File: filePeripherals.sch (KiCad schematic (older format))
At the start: 18 parts, among them J2 PP1_receptacle_TE_5-5530843-4, J3 PP1_receptacle_TE_5-5530843-4, J4 PP1_receptacle_TE_5-5530843-4, J5 PP1_receptacle_TE_5-5530843-4, U6 CD74AC238, U7 74AHC138

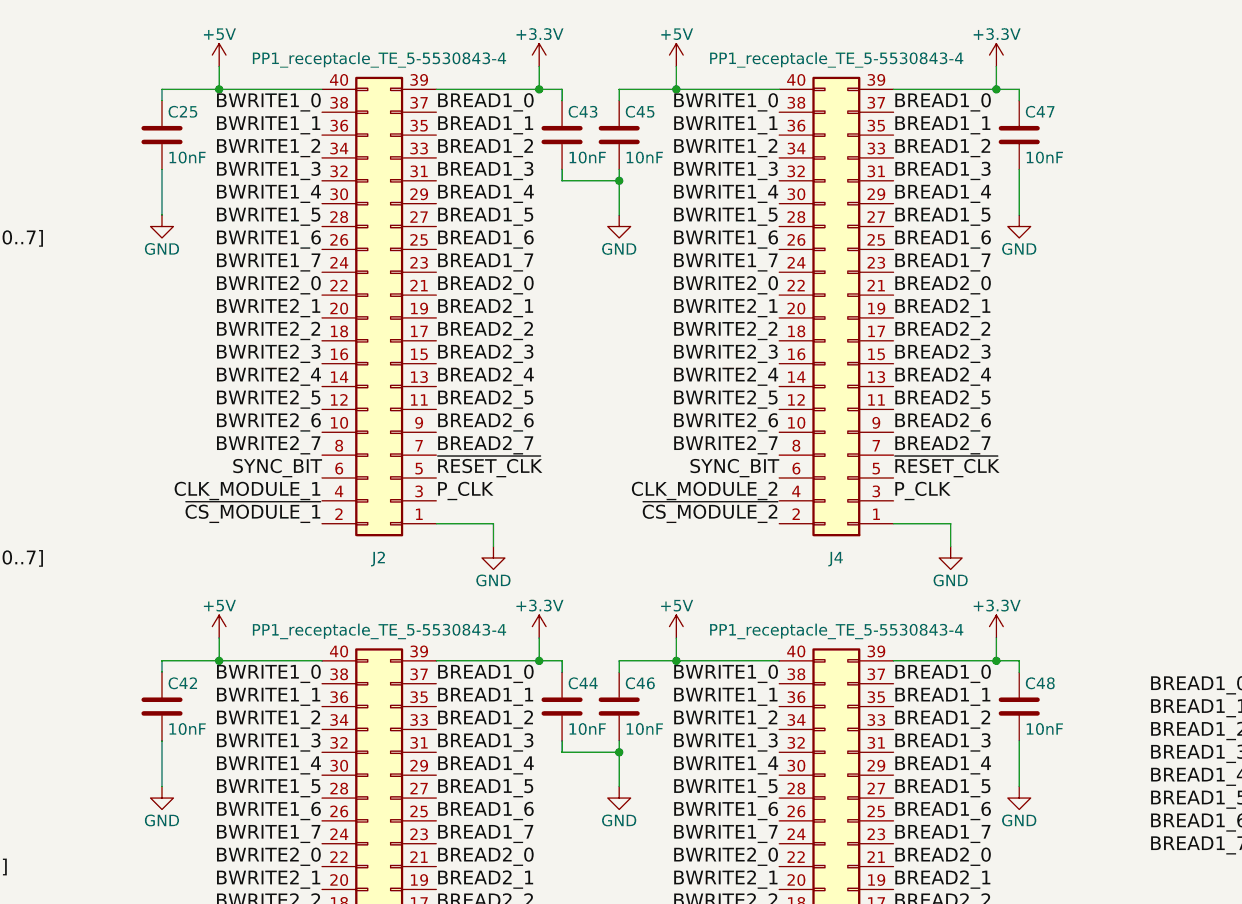
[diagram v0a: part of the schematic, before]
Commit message: V5.1 (#15)
* Remove compatibility for 5.0, 4.x and add 5.1+

* Fix switched pins on SN74LV393A #7

* Removed capacitor on 12V #11

* Add/Modify power decoupling capacitor #10

* Removing ADDSCR_CLK delay #9

* Schematics : set version 5.1, 2021 copyright and publish date

* Put non-electrolytic capacitor #10

* Set every capacitor size to 0805

* Add new footprint for J7 TE_3-641124-6 #6

* Schematic : set pinHeader on J12 #4

* Netlist, apply change to board, clean track, #6 #4 #12 #10

* Set version to 5.1, 2021 copyright and date, replace the missing QRcode

* Back the MM1 connectors #8

* Replace capacitor for U22 U23 U24 #13

* Better decoupling

* Increase version, year to 2021, clear status

* Precise the molex connector for power supply

* First step, import ses

* Clean bottom layer

* #14 Set the BWRITE2 bus instead of BWRITE1 on U12

* netlist, redo autorouting and cleaning

* use shields.io for colored badge

* Update gerbert files

* Changelog, updated BOM

* Small revision on blockDiagram

* Update README.md

* exporting pcb in pdf

* 3D images, diagram.png

* Update schematics pdf

* redo wavedrom_24bitsCounter
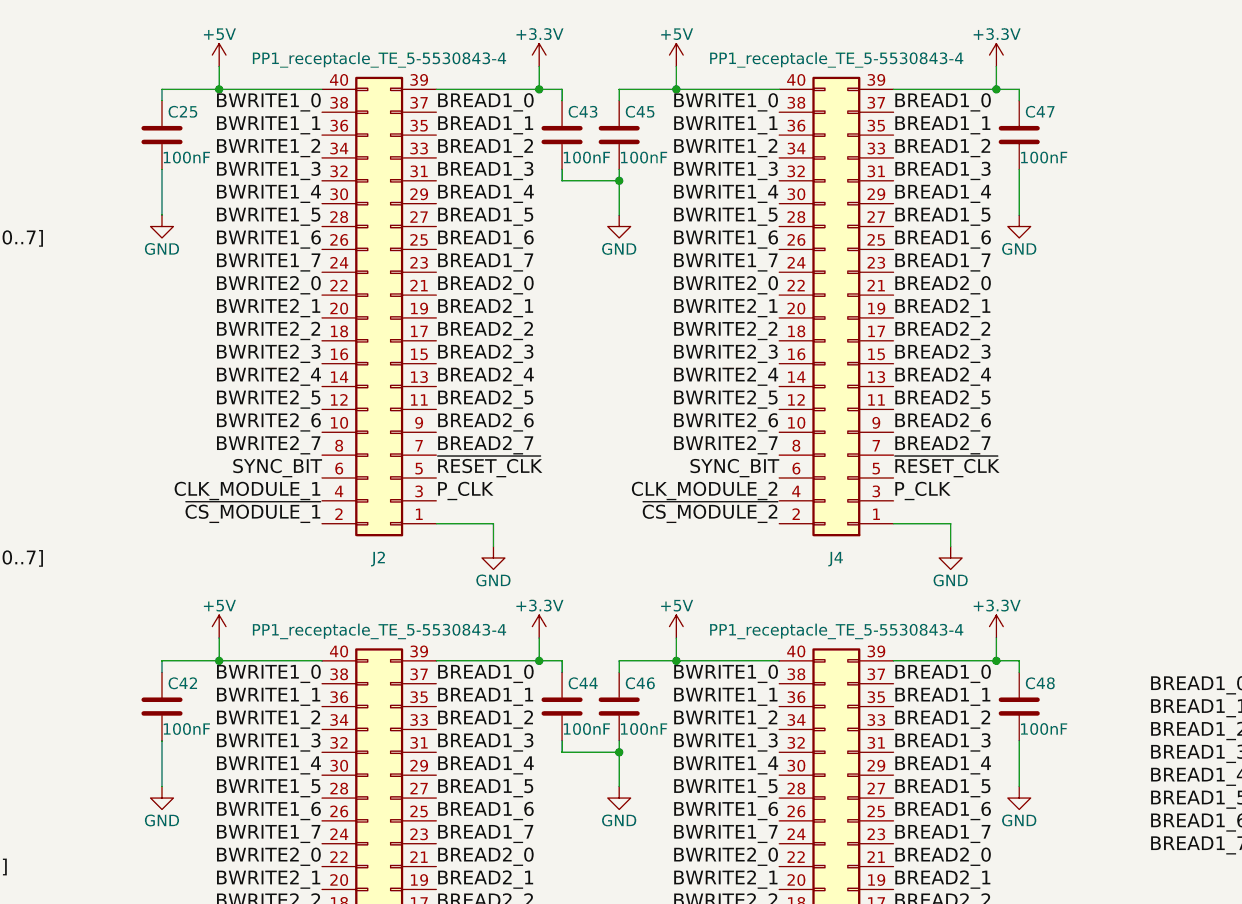
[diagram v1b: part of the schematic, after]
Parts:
- C25, C42, C43, C44, C45, C46, C47, C48: value 10nF -> 100nF
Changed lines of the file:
@@
 Sheet 2 10
 Title "GCM"
-Date "2020-11-23"
-Rev "V5.0"
+Date "2021-02-16"
+Rev "V5.1"
 Comp "Guillaume Guillet"
-Comment1 "Copyright Guillaume Guillet 2020"
+Comment1 "Copyright Guillaume Guillet 2021"
 Comment2 "Licensed under CERN-OHL-W v2 or later"
 Comment3 ""
@@
 AR Path="/5A97A24B/5C7994AC" Ref="C48"  Part="1"
 F 0 "C48" H 6525 3700 50  0000 L CNN
-F 1 "10nF" H 6525 3500 50  0000 L CNN
+F 1 "100nF" H 6500 3500 50  0000 L CNN
 F 2 "Capacitor_SMD:C_0805_2012Metric" H 6538 3450 50  0001 C CNN
 F 3 "" H 6500 3600 50  0001 C CNN
@@
 AR Path="/5A97A24B/5C799628" Ref="C44"  Part="1"
 F 0 "C44" H 4525 3700 50  0000 L CNN
-F 1 "10nF" H 4525 3500 50  0000 L CNN
+F 1 "100nF" H 4500 3500 50  0000 L CNN
 F 2 "Capacitor_SMD:C_0805_2012Metric" H 4538 3450 50  0001 C CNN
 F 3 "" H 4500 3600 50  0001 C CNN
@@
 AR Path="/5A97A24B/5C7996BA" Ref="C46"  Part="1"
 F 0 "C46" H 4775 3700 50  0000 L CNN
-F 1 "10nF" H 4775 3500 50  0000 L CNN
+F 1 "100nF" H 4750 3500 50  0000 L CNN
 F 2 "Capacitor_SMD:C_0805_2012Metric" H 4788 3450 50  0001 C CNN
 F 3 "" H 4750 3600 50  0001 C CNN
@@
 AR Path="/5A97A24B/5C799729" Ref="C42"  Part="1"
 F 0 "C42" H 2775 3700 50  0000 L CNN
-F 1 "10nF" H 2775 3500 50  0000 L CNN
+F 1 "100nF" H 2750 3500 50  0000 L CNN
 F 2 "Capacitor_SMD:C_0805_2012Metric" H 2788 3450 50  0001 C CNN
 F 3 "" H 2750 3600 50  0001 C CNN
@@
 AR Path="/5A97A24B/5C799DA9" Ref="C47"  Part="1"
 F 0 "C47" H 6525 1200 50  0000 L CNN
-F 1 "10nF" H 6525 1000 50  0000 L CNN
+F 1 "100nF" H 6500 1000 50  0000 L CNN
 F 2 "Capacitor_SMD:C_0805_2012Metric" H 6538 950 50  0001 C CNN
 F 3 "" H 6500 1100 50  0001 C CNN
@@
 AR Path="/5A97A24B/5C799F8A" Ref="C45"  Part="1"
 F 0 "C45" H 4775 1200 50  0000 L CNN
-F 1 "10nF" H 4775 1000 50  0000 L CNN
+F 1 "100nF" H 4750 1000 50  0000 L CNN
 F 2 "Capacitor_SMD:C_0805_2012Metric" H 4788 950 50  0001 C CNN
 F 3 "" H 4750 1100 50  0001 C CNN
@@
 AR Path="/5A97A24B/5C79A0DC" Ref="C43"  Part="1"
 F 0 "C43" H 4525 1200 50  0000 L CNN
-F 1 "10nF" H 4525 1000 50  0000 L CNN
+F 1 "100nF" H 4500 1000 50  0000 L CNN
 F 2 "Capacitor_SMD:C_0805_2012Metric" H 4538 950 50  0001 C CNN
 F 3 "" H 4500 1100 50  0001 C CNN
@@
 AR Path="/5A97A24B/5C79A155" Ref="C25"  Part="1"
 F 0 "C25" H 2775 1200 50  0000 L CNN
-F 1 "10nF" H 2775 1000 50  0000 L CNN
+F 1 "100nF" H 2750 1000 50  0000 L CNN
 F 2 "Capacitor_SMD:C_0805_2012Metric" H 2788 950 50  0001 C CNN
 F 3 "" H 2750 1100 50  0001 C CNN
